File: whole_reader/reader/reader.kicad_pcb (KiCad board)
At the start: 2 copper layers, 50 x 58.5 mm, 69 parts, among them U1 LM386M-1, U2 STM32F103C8T6, U3 MCP16301Hx-xCH, U4 TP3232N-SR, Y1 16MHz

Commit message: updates on pcb, bom file and experimenting with footprints
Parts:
- R2: footprint Potentiometer_SMD:Potentiometer_Bourns_3314S_Horizontal -> Potentiometer_SMD:Potentiometer_Bourns_3314G_Vertical
- RC522: footprint Connector_PinSocket_2.54mm:PinSocket_1x08_P2.54mm_Vertical -> UACS:PinSocket_1x08_P2.54mm_Vertical
- SWD1: footprint Connector_PinSocket_1.27mm:PinSocket_2x05_P1.27mm_Vertical -> UACS:PinSocket_2x05_P1.27mm_Vertical; moved to F.Cu
- moved RC522 8.71 mm to (145.5, 81.5), turned to 0 degrees
- moved SWD1 5.08 mm to (177.5, 57.3)
- moved R2 0.71 mm to (177.0, 37.5), turned to 0 degrees
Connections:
- SWD1 pad 1: +3.3V -> SWDIO
- SWD1 pad 10: NRST -> GND
- SWD1 pad 2: SWDIO -> +3.3V
- SWD1 pad 3: GND -> SWCLK
- SWD1 pad 4: SWCLK -> GND
- SWD1 pad 5: GND -> TRACESWO
- SWD1 pad 6: TRACESWO -> GND
- SWD1 pad 9: GND -> NRST
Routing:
- net Net-(R1-Pad2): track 11.0 -> 5.63 mm
- net Net-(U1-+): track 7.64 -> 6.10 mm
- net GND: track 57.5 -> 56.6 mm
- net NRST: track 94.9 -> 95.4 mm
- net LED_G2: track 51.3 -> 50.8 mm
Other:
- board text removed: "JLCJLCJLCJLC"

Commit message: Úprava popisov
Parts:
- moved H1 8.43 mm to (143.9, 34.0)
- moved G*** 3.23 mm to (142.7, 33.0)
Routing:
- net RFID_MISO: track 34.4 -> 33.5 mm
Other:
- board text added: "1.0 2025/04"
- board text added: "UACS-Reader"
- board text added: "Vol"
- board text removed: "UACS-Reader 1.0 2025/04"

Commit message: Otočenie potenciometra
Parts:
- moved R2 0.05 mm to (177.1, 37.5), turned to 180 degrees
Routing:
- net Net-(U1-+): track 6.10 -> 12.9 mm
- net GND: track 56.6 -> 60.6 mm, vias 210 -> 212
- net +3.3V: track 153.1 -> 152.4 mm
- net Net-(R1-Pad2): track 5.63 -> 6.28 mm
- net NRST: track 95.4 -> 94.8 mm

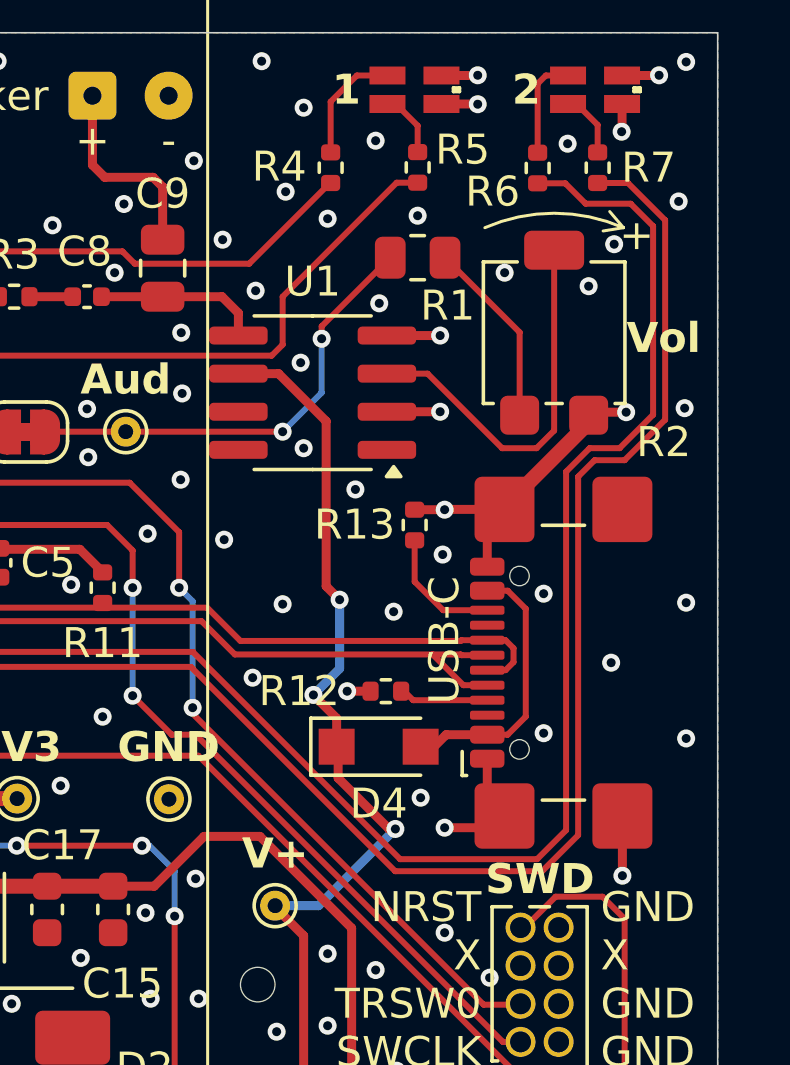
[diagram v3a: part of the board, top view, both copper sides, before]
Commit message: Posunutie USB-C konektora na kraj PCB podľa vyznačenej čiary
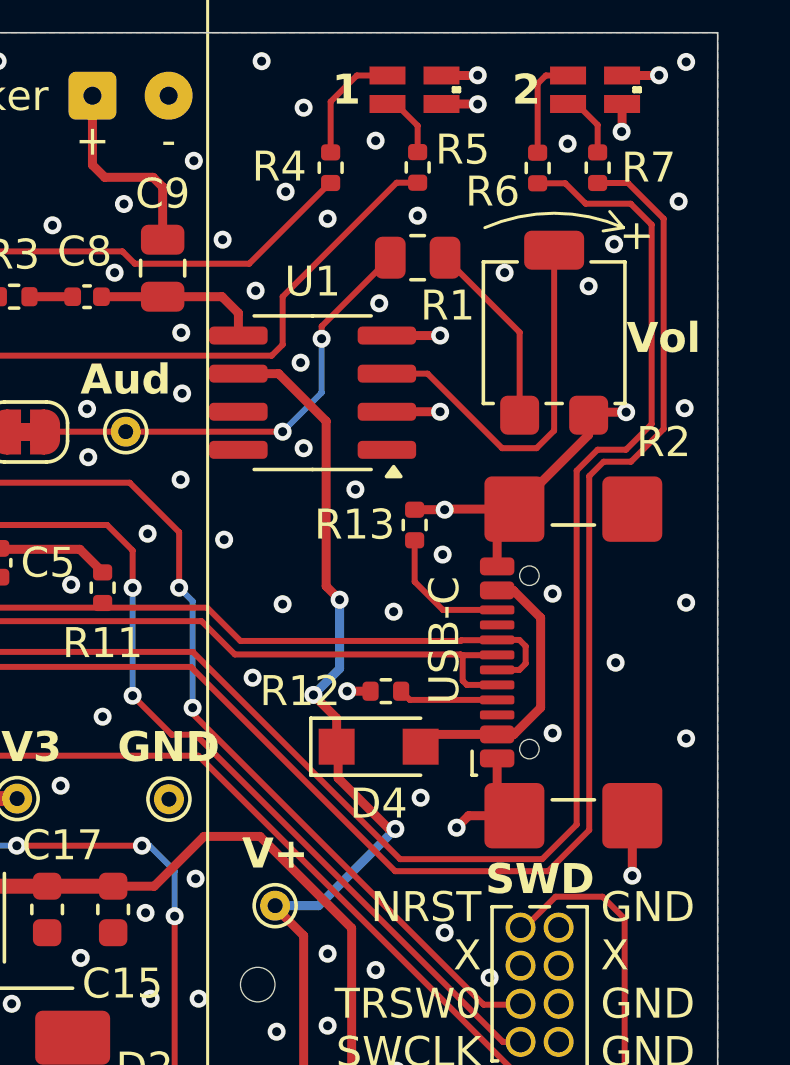
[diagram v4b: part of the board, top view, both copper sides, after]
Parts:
- moved USB-C1 0.33 mm to (178.8, 48.5)
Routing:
- net GND: track 60.6 -> 63.7 mm

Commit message: updated values and footprints of rezistors and other parts
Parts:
- C9: footprint Capacitor_SMD:C_0805_2012Metric -> Capacitor_SMD:C_1206_3216Metric
- R5: value 330 R -> 560 R; footprint Resistor_SMD:R_0402_1005Metric -> Resistor_SMD:R_0603_1608Metric
- R6: value 330 R -> 56 R
- R7: value 330 R -> 68 R
- R8, R9: footprint Resistor_SMD:R_0805_2012Metric -> Resistor_SMD:R_0603_1608Metric
- moved C9 0.55 mm to (164.0, 34.8)
- moved RC522 0.34 mm to (145.8, 81.5)
- moved R5 0.31 mm to (172.5, 32.3)
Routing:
- net Net-(U3-Vfb): track 9.42 -> 10.1 mm
- net RFID_MISO: track 33.5 -> 34.1 mm
- net GND: vias 212 -> 211

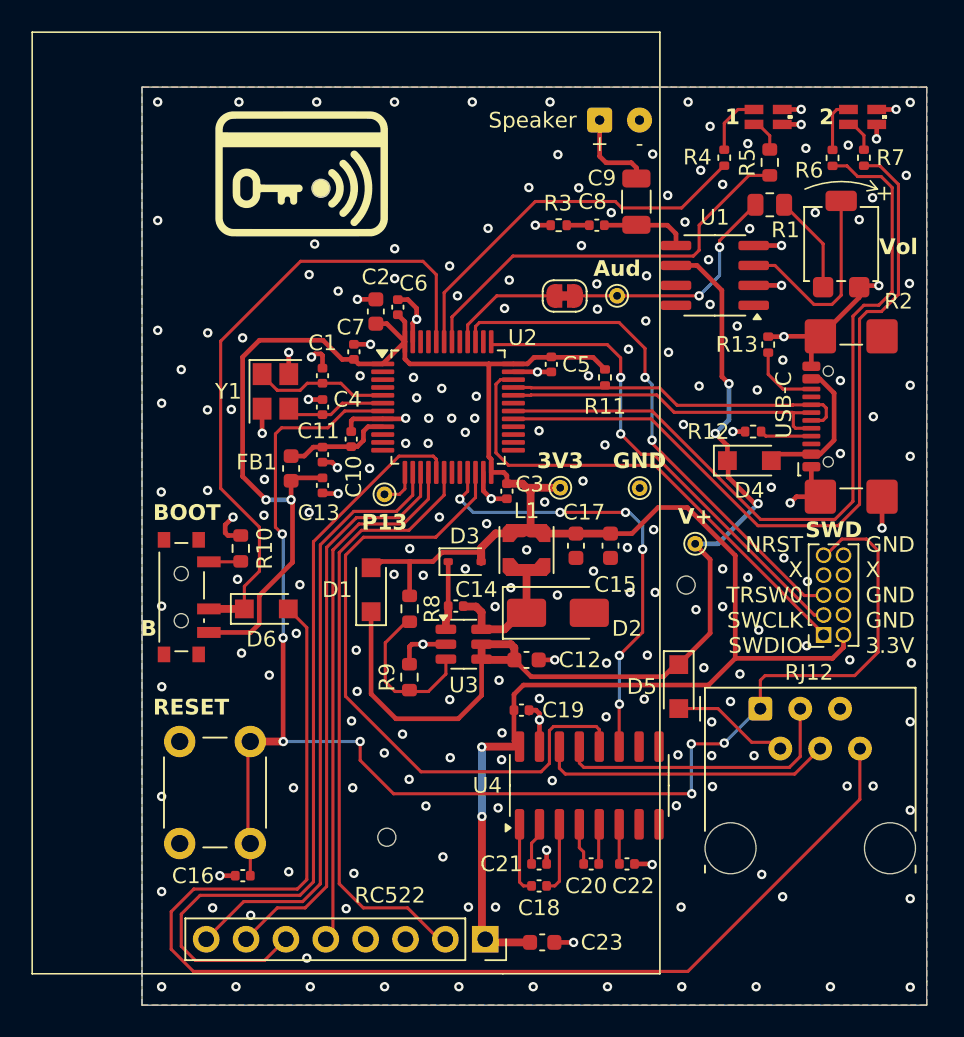
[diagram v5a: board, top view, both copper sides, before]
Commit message: add some vias
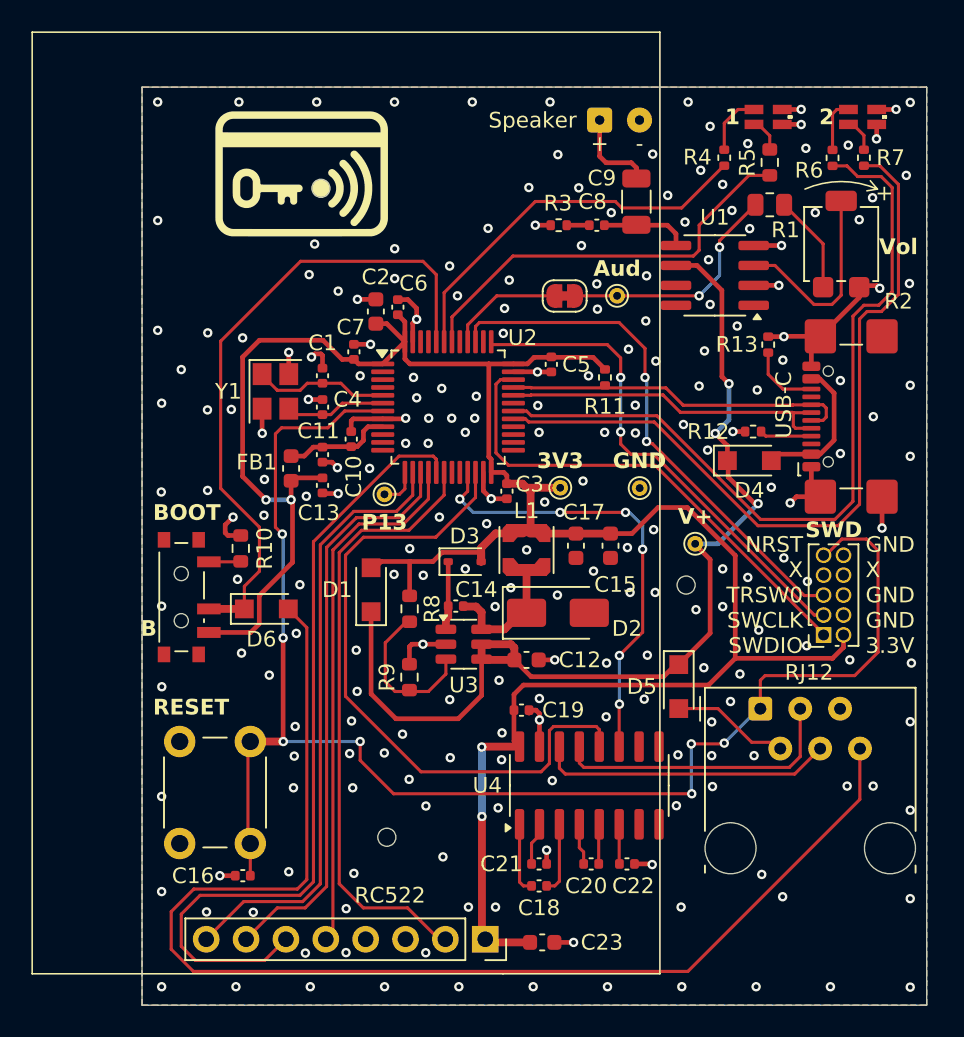
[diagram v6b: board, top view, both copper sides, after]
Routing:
- net GND: track 63.7 -> 62.1 mm, vias 211 -> 223
- net RFID_MISO: track 34.1 -> 33.4 mm

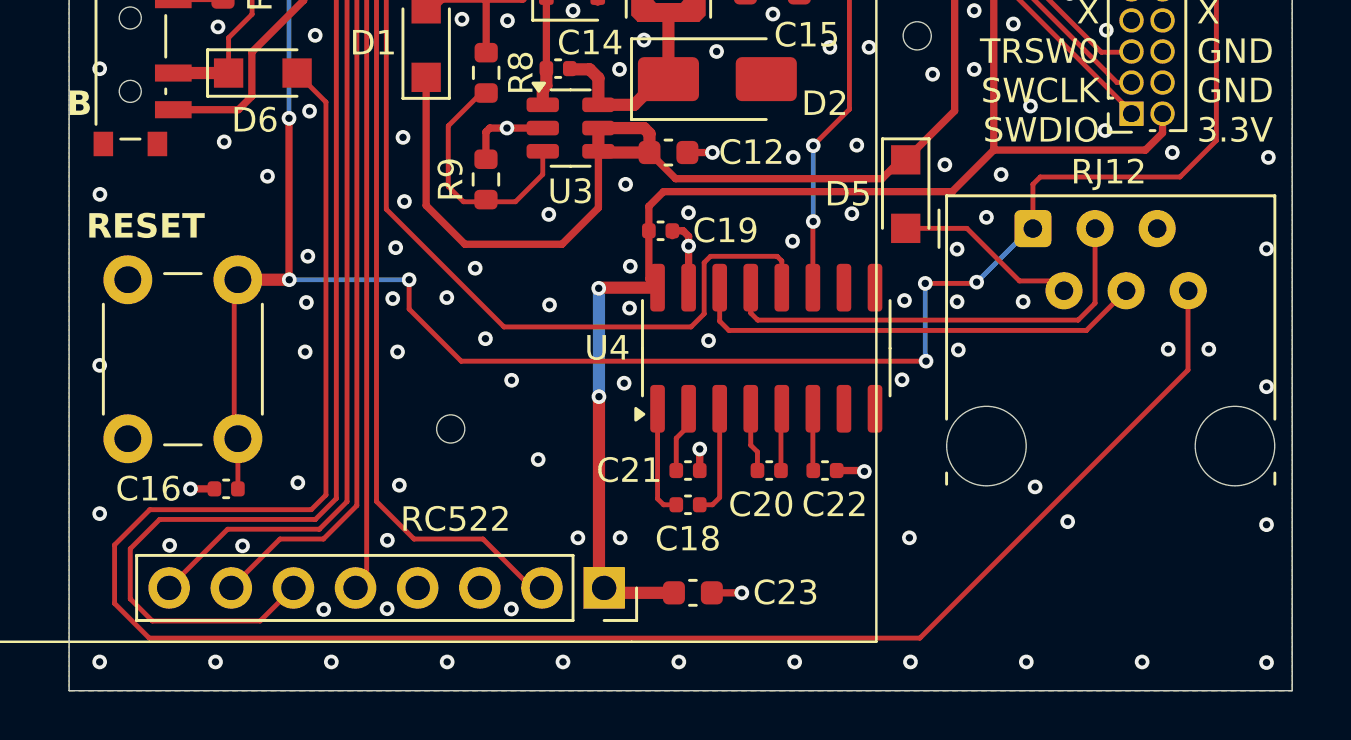
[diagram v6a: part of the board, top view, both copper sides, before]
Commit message: moved rj 12 connector
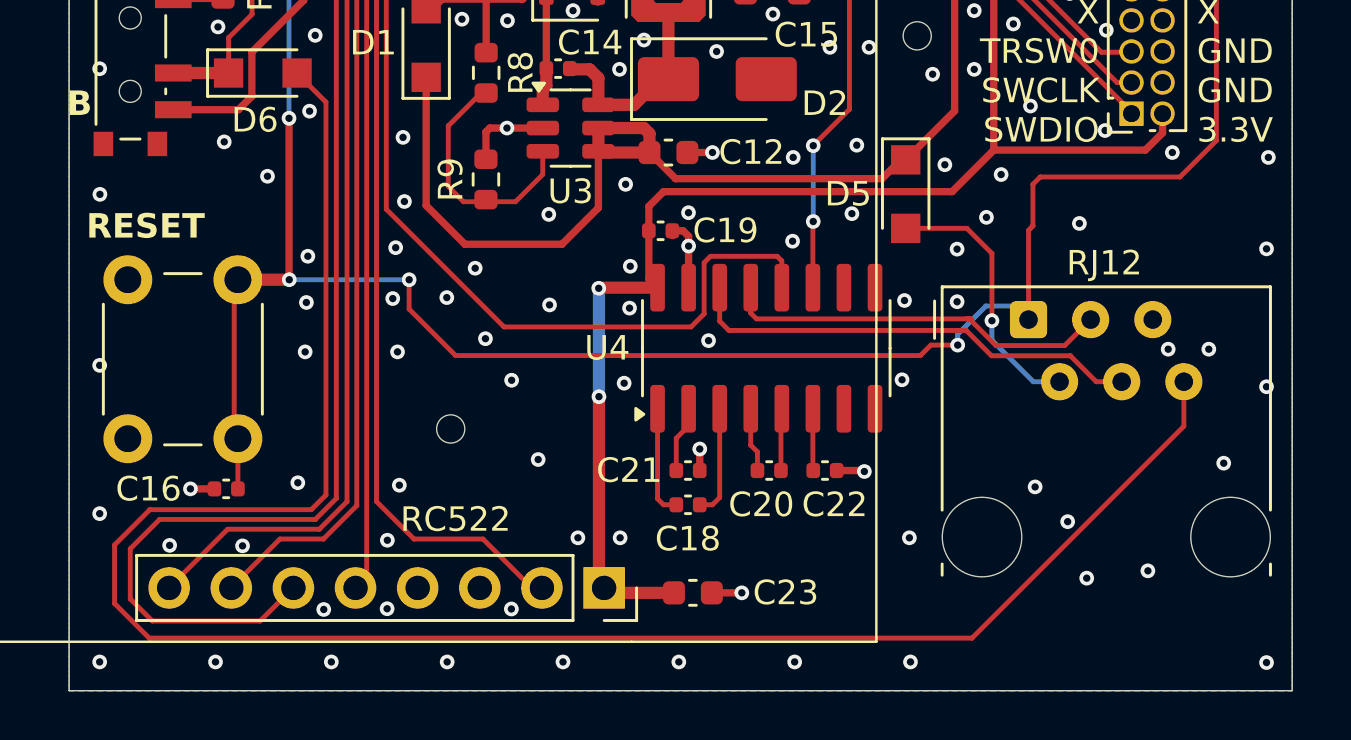
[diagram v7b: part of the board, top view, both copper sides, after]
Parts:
- moved RJ12 3.72 mm to (171.7, 70.8)
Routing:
- net Net-(D5-A): track 6.52 -> 10.5 mm, vias 0 -> 1
- net Net-(D6-A): track 81.8 -> 79.3 mm
- net Net-(U4-R1IN): track 18.2 -> 15.8 mm
- net NRST: track 94.8 -> 95.7 mm, vias 7 -> 5
- net GND: vias 223 -> 222

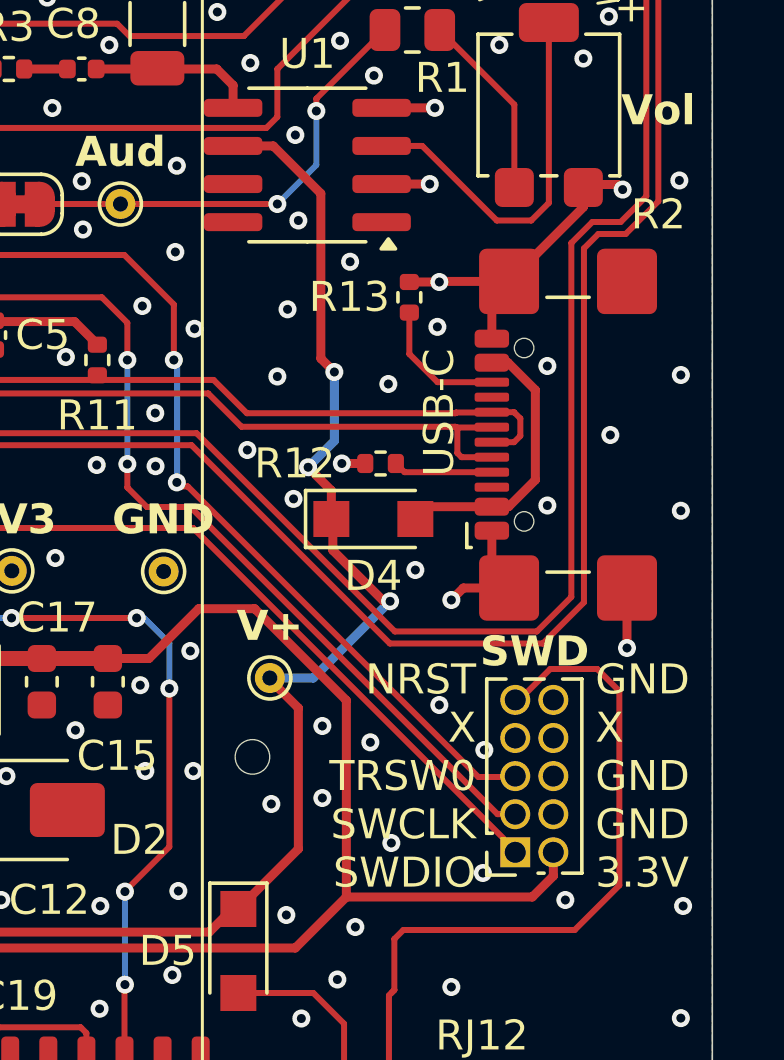
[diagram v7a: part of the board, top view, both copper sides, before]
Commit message: changed rotations of components
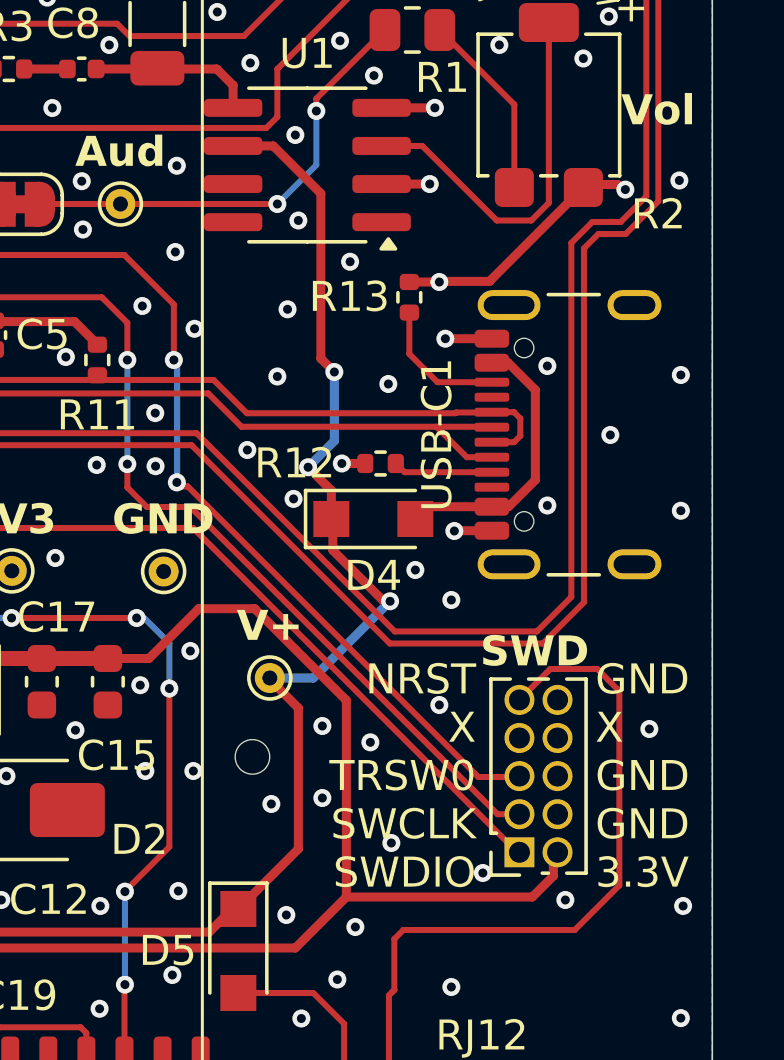
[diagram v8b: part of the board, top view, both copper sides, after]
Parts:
- USB-C1: footprint Connector_USB:USB_C_Receptacle_GCT_USB4110 -> Connector_USB:USB_C_Receptacle_GCT_USB4105-xx-A_16P_TopMnt_Horizontal
- moved SWD1 3.63 mm to (174.3, 59.1), turned to 90 degrees
- turned LED1 to 180 degrees
- turned LED2 to 180 degrees
- turned R2 to 0 degrees
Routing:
- net GND: track 62.1 -> 57.8 mm
- net USB_D-: track 21.2 -> 21.7 mm
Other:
- board text removed: "USB-C"
